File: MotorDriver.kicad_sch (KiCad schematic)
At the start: 3 parts, among them U1 DRV8323HRTAR

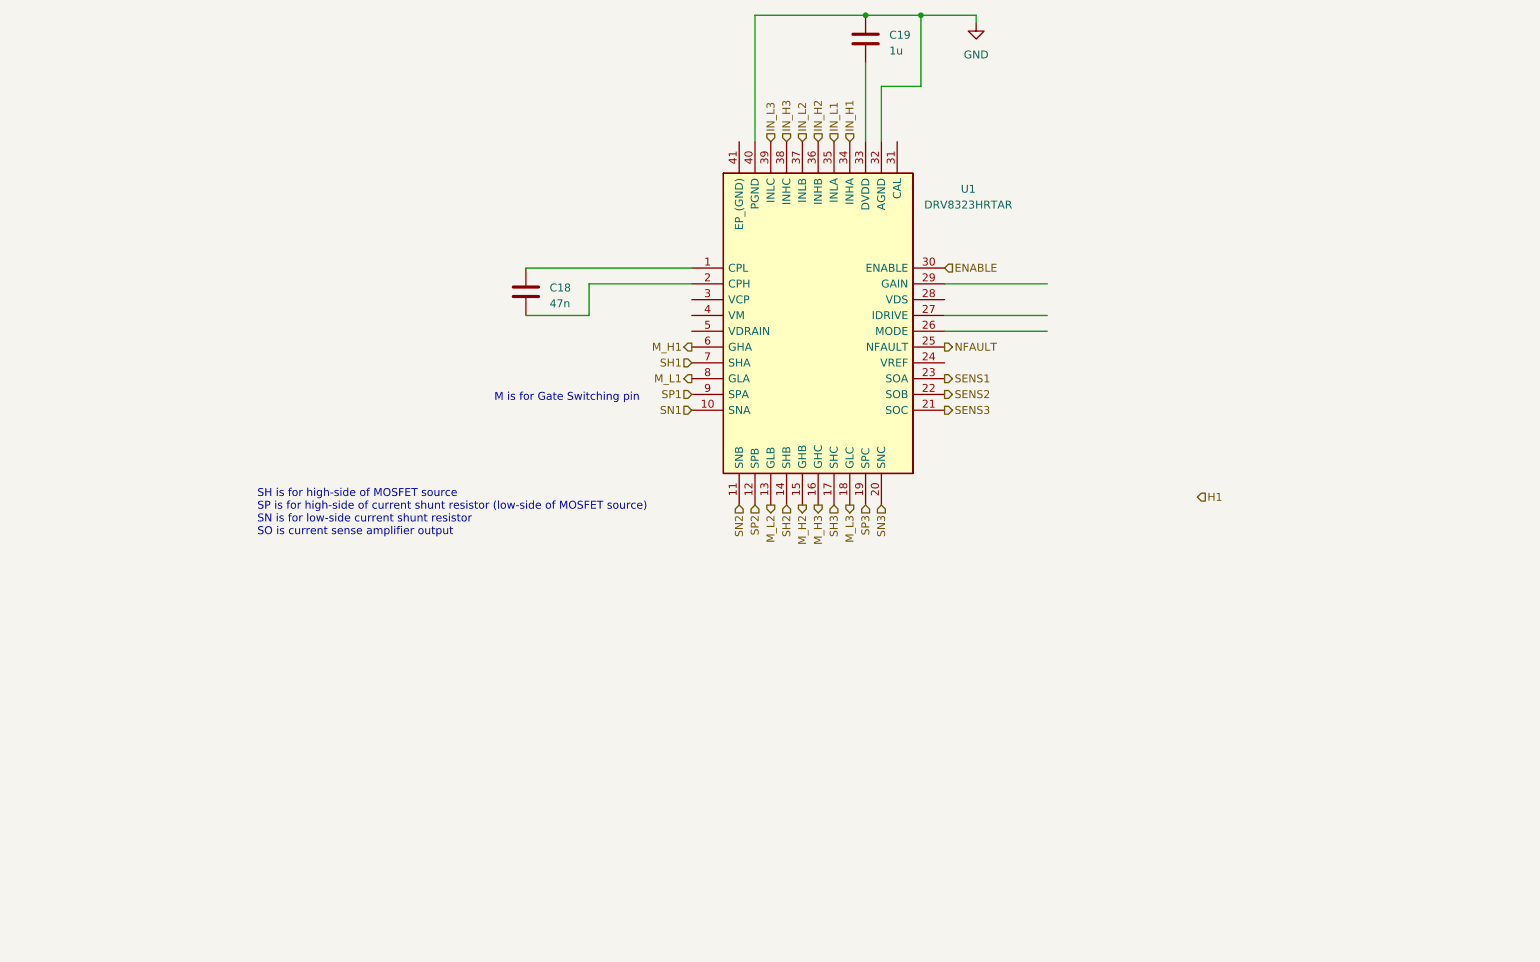
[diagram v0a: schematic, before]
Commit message: Add MotorDriver schematic sheet
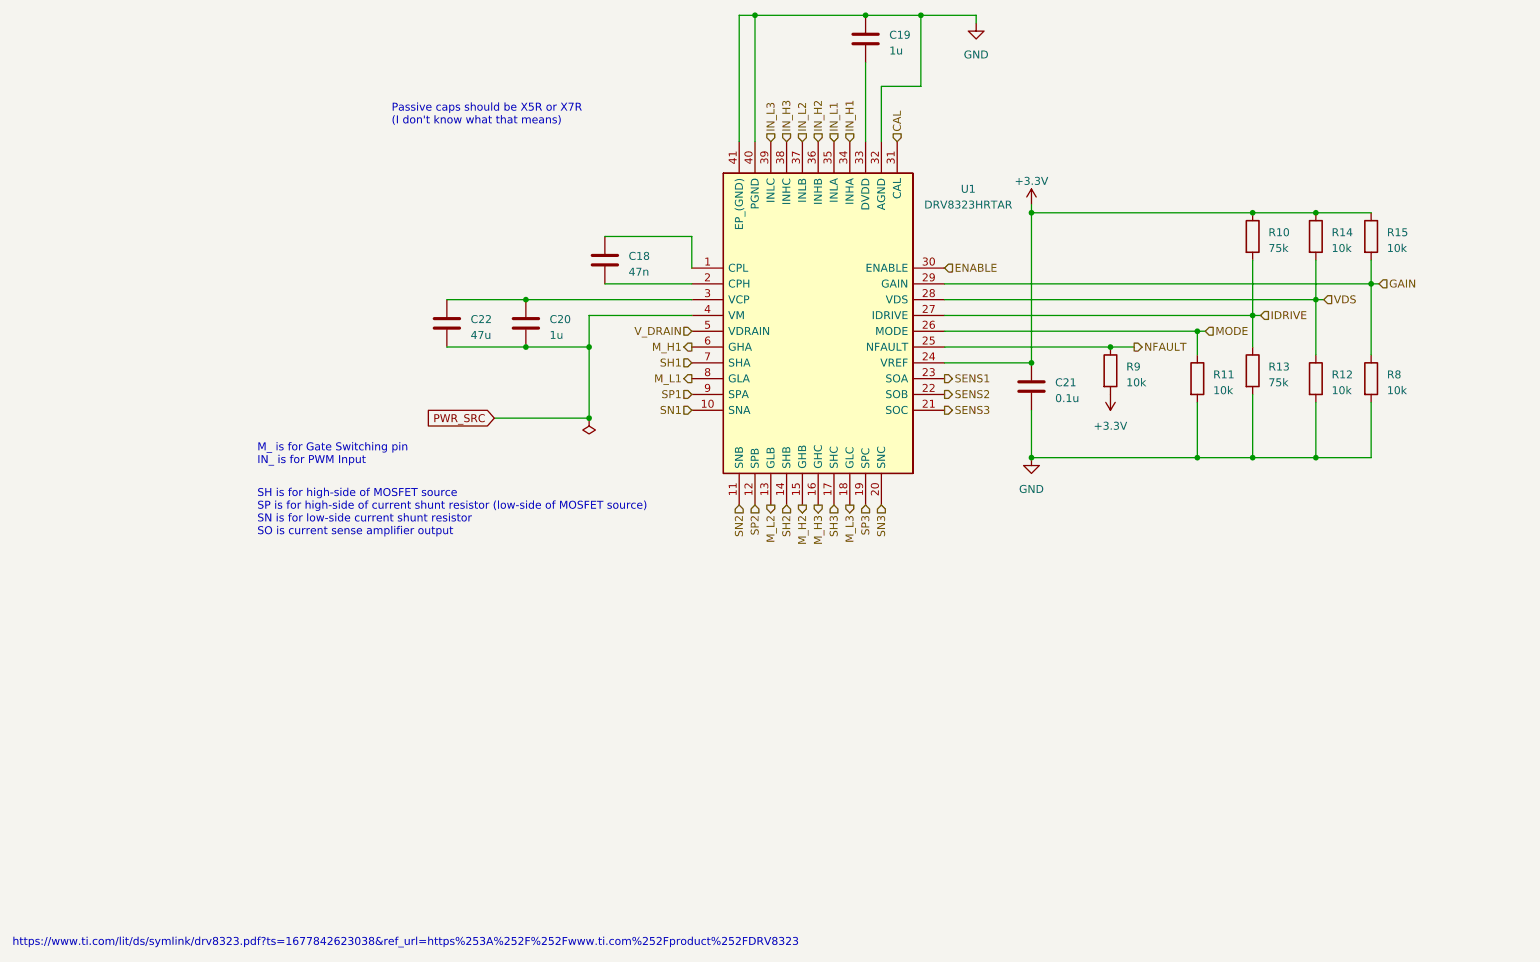
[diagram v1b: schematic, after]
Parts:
- added C20: 1u, symbol Device:C
- added C21: 0.1u, symbol Device:C
- added C22: 47u, symbol Device:C
- added R10, R13: 75k, symbol Device:R
- added R11, R12, R14, R15, R8, R9: 10k, symbol Device:R
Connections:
- net GND: now also U1.41 (EP_(GND)), C21.2, R11.2, R12.2, R13.2, R8.2
- net NFAULT: now also R9.1
- net +3.3V: now reaches U1.24 (VREF)
- net +3.3V: now also C21.1, R10.1, R14.1, R15.1, R9.2
- net MODE: now reaches U1.26 (MODE)
- net MODE: now also R11.1
- net IDRIVE: now reaches U1.27 (IDRIVE)
- net IDRIVE: now also R10.2, R13.1
- net VDS: now reaches U1.28 (VDS)
- net VDS: now also R12.1, R14.2
- net GAIN: now reaches U1.29 (GAIN)
- net GAIN: now also R15.2, R8.1
- net at U1.3 (VCP): now also C20.1, C22.1
- net CAL: now reaches U1.31 (CAL)
- net PWR_SRC: now reaches U1.4 (VM)
- net PWR_SRC: now also C20.2, C22.2
- net V_DRAIN: now reaches U1.5 (VDRAIN)
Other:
- note added: "M_ is for Gate Switching pin IN_ is for PWM Input"
- note added: "Passive caps should be X5R or X7R (I don't know what that means)"
- note added: "https://www.ti.com/lit/ds/symlink/drv8323.pdf?ts=1677842623038&ref_url=https%253A%252F%252Fwww.ti.com%252Fproduct%252FDRV8323"
- note removed: "M is for Gate Switching pin"
- moved on the sheet: C18

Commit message: Remove dup folder
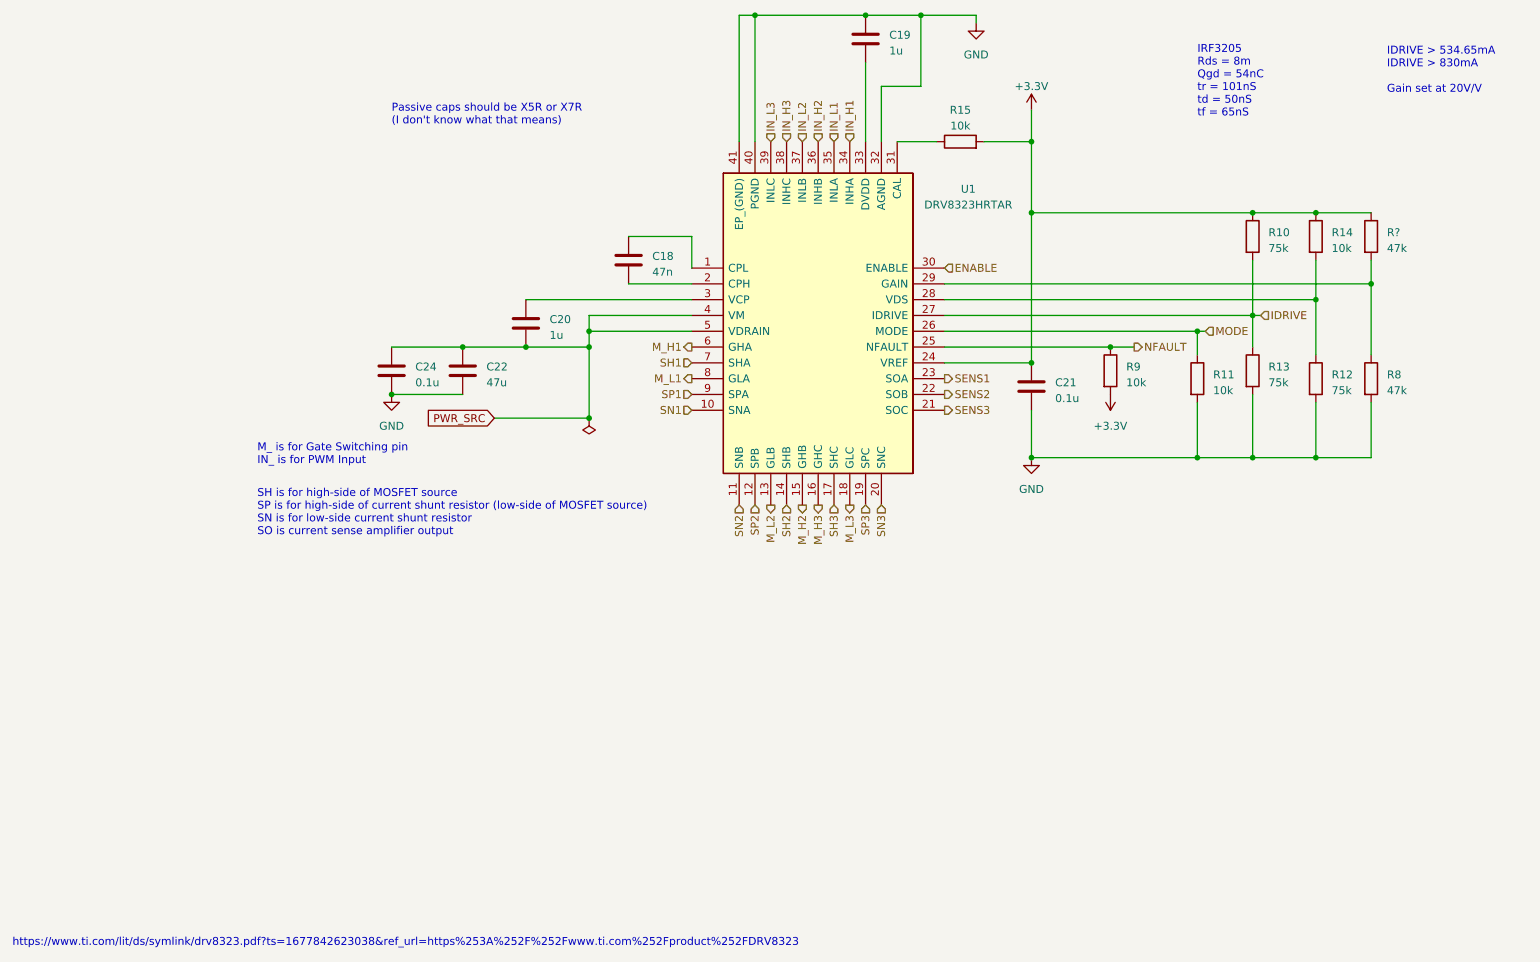
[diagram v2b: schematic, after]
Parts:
- added C24: 0.1u, symbol Device:C
- added R15: 10k, symbol Device:R
- R12: value 10k -> 75k
- R8: value 10k -> 47k
- R?: renamed from R15; value 10k -> 47k
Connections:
- net V_DRAIN is gone; now on net PWR_SRC: U1.5 (VDRAIN)
- net +3.3V: now also R15.2
- net GND: now also C22.2, C24.2
- net PWR_SRC: now also C22.1, C24.1; no longer C22.2
- net at C20.1, U1.3 (VCP): no longer C22.1
- net CAL: no longer names the net of U1.31 (CAL)
- net CAL: now also R15.1
- net GAIN: no longer names the net of R8.1, R?.2, U1.29 (GAIN)
- net VDS: no longer names the net of R12.1, R14.2, U1.28 (VDS)
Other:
- note added: "IDRIVE > 534.65mA IDRIVE > 830mA Gain set at 20V/V"
- note added: "IRF3205 Rds = 8m Qgd = 54nC tr = 101nS td = 50nS tf = 65nS"
- moved on the sheet: C18, C22
